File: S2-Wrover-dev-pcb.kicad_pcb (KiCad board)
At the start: 2 copper layers, 99.1 x 50 mm, 6 parts, among them P1 CONN_02X13

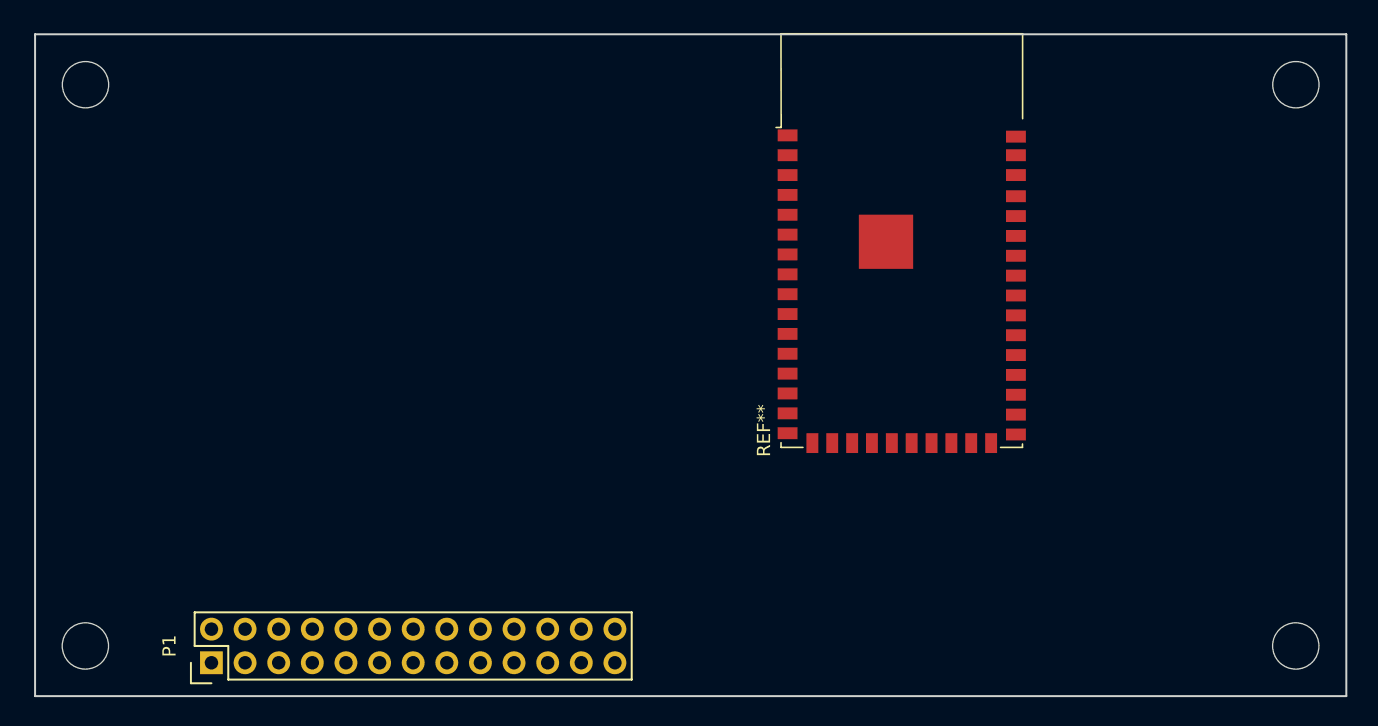
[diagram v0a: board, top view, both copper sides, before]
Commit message: Update schematic and assign footprints
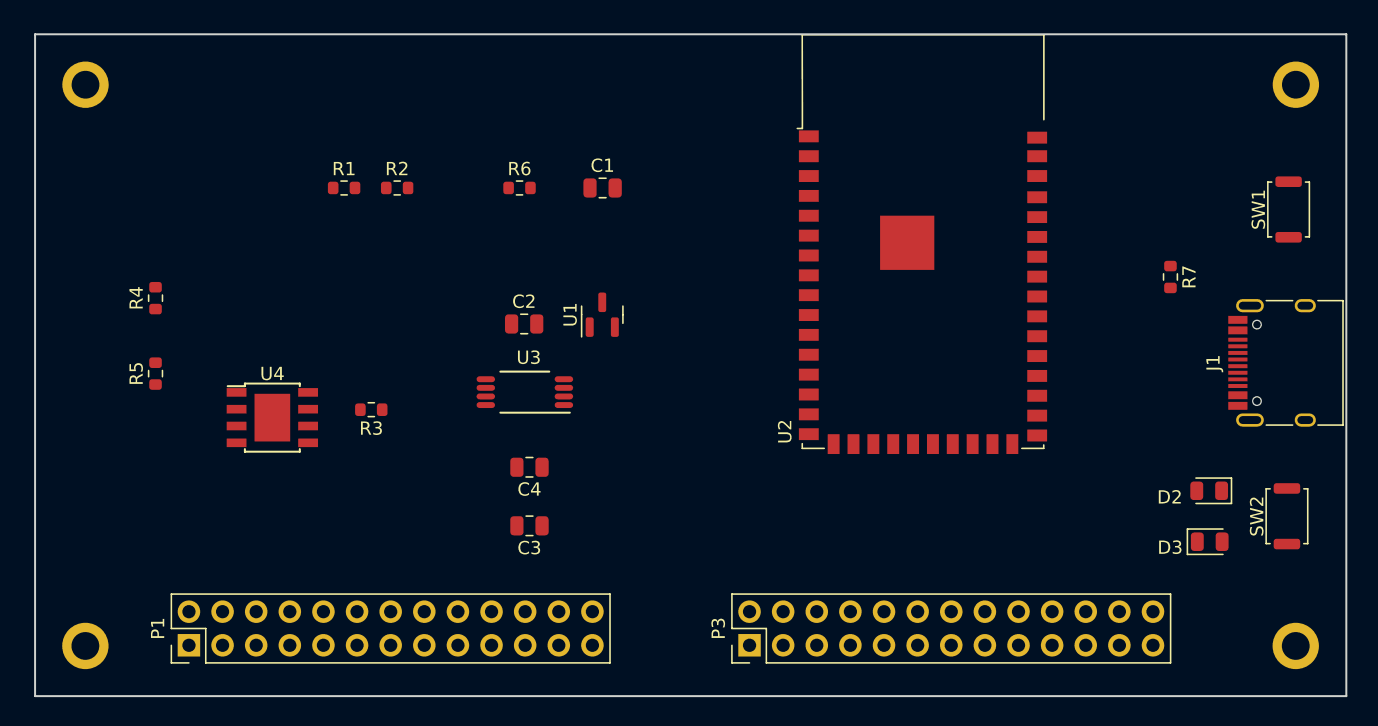
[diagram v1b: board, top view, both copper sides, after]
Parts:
- removed REF**: ESP32-S2-WROVER, footprint:ESP32-S2-WROVER
- added C1: 0.1u, Capacitor_SMD:C_0805_2012Metric, F.Cu at (139.4, 82.7)
- added C2: 100nF, Capacitor_SMD:C_0805_2012Metric, F.Cu at (133.5, 93.0)
- added C3: 100nF, Capacitor_SMD:C_0805_2012Metric, F.Cu at (133.9, 108.3)
- added C4: 100nF, Capacitor_SMD:C_0805_2012Metric, F.Cu at (133.9, 103.8)
- added D2: GRE, LED_SMD:LED_0805_2012Metric, F.Cu at (185.2, 105.6)
- added D3: RED, LED_SMD:LED_0805_2012Metric, F.Cu at (185.3, 109.5)
- added J1: USB_C_Receptacle_USB2.0, footprint:USB_C_Receptacle_HRO_TYPE-C-31-M-12, F.Cu at (191.4, 95.9)
- added P3: CONN_02X13, Connector_PinHeader_2.54mm:PinHeader_2x13_P2.54mm_Vertical, F.Cu at (150.5, 117.3)
- added R1: 10K, Resistor_SMD:R_0603_1608Metric, F.Cu at (119.9, 82.7)
- added R2: 1K, Resistor_SMD:R_0603_1608Metric, F.Cu at (123.9, 82.7)
- added R3: 1K, Resistor_SMD:R_0603_1608Metric, F.Cu at (121.9, 99.5)
- added R4: 400, Resistor_SMD:R_0603_1608Metric, F.Cu at (105.6, 91.1)
- added R5: 6.8K, Resistor_SMD:R_0603_1608Metric, F.Cu at (105.6, 96.8)
- added R6: 5.1k, Resistor_SMD:R_0603_1608Metric, F.Cu at (133.1, 82.7)
- added R7: 5.1k, Resistor_SMD:R_0603_1608Metric, F.Cu at (182.3, 89.5)
- added SW1: RESET, footprint:Alps_SKRK, F.Cu at (191.2, 84.4)
- added SW2: BOOT, footprint:Alps_SKRK, F.Cu at (191.1, 107.5)
- added U1: MCP1700-1202E_SOT23, Package_TO_SOT_SMD:SOT-23, F.Cu at (139.4, 92.3)
- added U2: ESP32-S2-WROVER, RF_Module:ESP32-S2-WROVER, F.Cu at (163.6, 90.6)
- added U3: Val**, footprint:TPS2113APW, F.Cu at (133.5, 98.2)
- added U4: TP4056, TP4056:TP4056_SOP-8-PP, F.Cu at (114.4, 100.1)
- P1: footprint Pin_Headers:Pin_Header_Straight_2x13 -> Connector_PinHeader_2.54mm:PinHeader_2x13_P2.54mm_Vertical
- moved P1 2.15 mm to (108.1, 117.3)
- renumbered MK4 to MK2
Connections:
- P1 pad 1: GND -> BAT-
- P1 pad 10: GPIO_UART1_CTS -> /IO04
- P1 pad 11: GPIO_SPI_CLK -> unconnected-(P1-Pad11)
- P1 pad 12: GPIO_UART1_RTS -> /IO05
- P1 pad 13: GPIO_I2C_SCL -> unconnected-(P1-Pad13)
- P1 pad 14: GPIO_I2S_CLK -> /IO06
- P1 pad 15: GPIO_I2C_SDA -> unconnected-(P1-Pad15)
- P1 pad 16: GPIO_I2S_FRM -> /IO07
- P1 pad 17: GPIO_UART2_TXD -> unconnected-(P1-Pad17)
- P1 pad 18: GPIO_I2S_DO -> /IO08
- P1 pad 19: GPIO_UART2_RXD -> unconnected-(P1-Pad19)
- P1 pad 2: GND -> /3.3v
- P1 pad 20: GPIO_I2S_DI -> /IO09
- P1 pad 21: GPIO_S5_0 -> unconnected-(P1-Pad21)
- P1 pad 22: GPIO_PWM0 -> /IO10
- P1 pad 23: GPIO_S5_1 -> unconnected-(P1-Pad23)
- P1 pad 24: GPIO_PWM1 -> /IO11
- P1 pad 25: GPIO_S5_2 -> unconnected-(P1-Pad25)
- P1 pad 26: I2SMCLK_GPIO -> /IO12
- P1 pad 3: +5V -> unconnected-(P1-Pad3)
- P1 pad 4: +3V3 -> /IO01
- P1 pad 5: GPIO_SPI_CS# -> unconnected-(P1-Pad5)
- P1 pad 6: GPIO_UART1_TXD -> /IO02
- P1 pad 7: GPIO_SPI_MISO -> unconnected-(P1-Pad7)
- P1 pad 8: GPIO_UART1_RXD -> /IO03
- P1 pad 9: GPIO_SPI_MOSI -> unconnected-(P1-Pad9)

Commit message: Update schematic
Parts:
- added J2: Jack-DC, Connector_JST:JST_EH_S2B-EH_1x02_P2.50mm_Horizontal, F.Cu at (112.2, 82.0)
- added P_DEV: CONN_02X13, Connector_PinHeader_2.54mm:PinHeader_2x13_P2.54mm_Vertical, F.Cu at (108.4, 117.3)
- U3: value Val** -> TPS2113APW
- moved C4 13.2 mm to (138.9, 91.6)
- moved C3 13.2 mm to (138.9, 96.1)
- moved R4 9.60 mm to (107.7, 81.7)
- moved R5 9.60 mm to (107.7, 87.4)
- moved R3 9.35 mm to (121.9, 90.1)
- moved U4 9.35 mm to (114.4, 90.7)
- moved U1 8.96 mm to (138.6, 83.4)
- moved C2 8.96 mm to (132.7, 84.1)
- moved U3 8.96 mm to (132.8, 89.2)
- moved P1 6.63 mm to (108.4, 110.7)
- moved D2 4.32 mm to (181.1, 104.4)
- moved D3 4.32 mm to (181.1, 108.3)
- moved R1 4.03 mm to (119.9, 78.7)
- moved R2 4.03 mm to (124.0, 78.7)
- moved C1 3.66 mm to (138.7, 79.1)
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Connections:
- net BAT- renamed GND
- net Net-(U1-Pad3) renamed VIN
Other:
- board text added: "ESP32S2 WROVER SOC idf.py dfu dfu-flash"
- board text added: "FASANI CORPORATION"
- board text added: "FREE AREA"

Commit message: V1 wiring
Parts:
- added C5: 0.1u, Capacitor_SMD:C_0805_2012Metric, F.Cu at (177.0, 78.9)
- moved R1 61.3 mm to (181.2, 80.6)
- moved R2 60.4 mm to (179.3, 102.9), turned to 180 degrees
- moved R3 59.8 mm to (179.8, 105.3), turned to 0 degrees
- moved R6 52.8 mm to (181.7, 98.1)
- moved C1 42.8 mm to (181.3, 83.1), turned to 180 degrees
- moved U1 16.4 mm to (126.5, 94.5)
- moved C3 12.2 mm to (144.3, 85.1)
- moved P3 6.07 mm to (146.0, 113.2)
- moved C4 5.98 mm to (144.3, 89.1)
- moved U4 4.63 mm to (119.1, 90.8), turned to 90 degrees
- moved J2 3.98 mm to (116.2, 81.7)
- moved R5 3.65 mm to (111.3, 88.0)
- moved R4 3.65 mm to (111.3, 82.3)
- moved U3 2.48 mm to (132.9, 91.7), turned to 90 degrees
- moved D3 2.35 mm to (183.2, 107.2)
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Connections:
- P3 pad 10: /IO15 -> /IO17
- P3 pad 12: /IO16 -> /IO18
- P3 pad 14: /IO17 -> /IO21
- P3 pad 16: /IO21 -> /IO33
- P3 pad 18: /IO33 -> /IO34
- P3 pad 20: /IO34 -> /IO35
- P3 pad 22: /IO35 -> /IO36
- P3 pad 24: /IO36 -> /IO37
- P3 pad 26: /IO37 -> unconnected-(P3-Pad26)
- P3 pad 8: /IO14 -> /IO16
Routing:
- net GND: track 0.00 -> 157.4 mm, vias 0 -> 6
- net Net-(R3-Pad2): track 0.00 -> 154.7 mm, vias 0 -> 4
- net VBUS: track 0.00 -> 153.3 mm, vias 0 -> 6
- net /3.3v: track 0.00 -> 131.6 mm, vias 0 -> 5
- net /IO46: track 0.00 -> 85.5 mm, vias 0 -> 1
- net Net-(R2-Pad2): track 0.00 -> 84.9 mm, vias 0 -> 2
- net /IO45: track 0.00 -> 80.5 mm, vias 0 -> 1
- net /IO41: track 0.00 -> 77.8 mm, vias 0 -> 2
- net BOOT_MODE: track 0.00 -> 72.2 mm, vias 0 -> 4
- net /IO42: track 0.00 -> 67.5 mm, vias 0 -> 2
- net /IO40: track 0.00 -> 66.3 mm, vias 0 -> 2
- net /RX: track 0.00 -> 59.9 mm, vias 0 -> 1
- net /IO01: track 0.00 -> 56.4 mm
- net /IO02: track 0.00 -> 53.5 mm
- net /TX: track 0.00 -> 51.2 mm, vias 0 -> 1
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
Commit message: Passing DRC
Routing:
- net GND: track 157.4 -> 196.5 mm, vias 6 -> 13
- net VBUS: track 153.3 -> 150.7 mm
- net /IO10: track 29.7 -> 28.4 mm
- net /IO16: track 12.0 -> 11.2 mm
- net /IO12: track 23.2 -> 22.4 mm
- net /IO15: track 12.3 -> 11.6 mm
- net /IO13: track 15.6 -> 14.9 mm
- net /IO14: track 13.6 -> 13.0 mm
- net /IO08: track 36.3 -> 35.7 mm
- net /IO42: track 67.5 -> 68.0 mm
- added copper zone on B.Cu, net GND
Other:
- outline, holes or cut-outs redrawn

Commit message: Make only one big GND pane in bottom layer
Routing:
- net GND: vias 13 -> 16
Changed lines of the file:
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@@
       (effects (font (size 1 1) (thickness 0.15)))
     )
-    (fp_text value "ESP32-S2-WROVER" (at 0.145 -8.075 180) (layer "F.Fab")
+    (fp_text value "ESP32-S2-WROVER" (at 0.22 -13.8 180) (layer "F.Fab")
       (effects (font (size 1 1) (thickness 0.15)))
     )
@@
   (segment (start 187.385 92.5375) (end 188.3 91.6225) (width 0.4) (layer "F.Cu") (net 1))
   (via (at 132.12 96.005) (size 0.6) (drill 0.4) (layers "F.Cu" "B.Cu") (net 1))
+  (via (at 161.42 86.78) (size 0.8) (drill 0.6) (layers "F.Cu" "B.Cu") (net 1))
   (via (at 133.77 81.78) (size 0.6) (drill 0.4) (layers "F.Cu" "B.Cu") (net 1))
   (via (at 140.845 108.805) (size 0.6) (drill 0.4) (layers "F.Cu" "B.Cu") (net 1))
@@
   (via (at 183.77 94.555) (size 0.6) (drill 0.4) (layers "F.Cu" "B.Cu") (net 1))
   (via (at 108.595 87.08) (size 0.6) (drill 0.4) (layers "F.Cu" "B.Cu") (net 1))
+  (via (at 162.4575 86.78) (size 0.8) (drill 0.6) (layers "F.Cu" "B.Cu") (net 1))
   (via (at 183.995 82.605) (size 0.6) (drill 0.4) (layers "F.Cu" "B.Cu") (net 1))
   (via (at 134.745 87.43) (size 0.6) (drill 0.4) (layers "F.Cu" "B.Cu") (net 1))
   (via (at 184.5575 92.6925) (size 0.6) (drill 0.4) (layers "F.Cu" "B.Cu") (net 1))
+  (via (at 163.495 86.805) (size 0.8) (drill 0.6) (layers "F.Cu" "B.Cu") (net 1))
   (segment (start 113.92 87.13) (end 108.645 87.13) (width 0.3) (layer "B.Cu") (net 1))
   (segment (start 132.12 96.005) (end 129.595 96.005) (width 0.4) (layer "B.Cu") (net 1))
@@
   (segment (start 191.195 90.48) (end 191.195 109.555) (width 0.25) (layer "B.Cu") (net 55))
   (zone (net 1) (net_name "GND") (layer "B.Cu") (hatch edge 0.508)
-    (connect_pads (clearance 0))
+    (connect_pads (clearance 0.4))
     (min_thickness 0.254) (filled_areas_thickness no)
     (fill yes (thermal_gap 0.508) (thermal_bridge_width 0.508))
     (polygon
       (pts
-        (xy 153.47 108.905)
+        (xy 195.97 121.355)
+        (xy 178.245 121.33)
+        (xy 178.245 108.78)
+        (xy 170.3575 108.78)
         (xy 144.845 108.905)
         (xy 144.595 114.105)
@@
         (xy 95.92 109.155)
         (xy 95.87 70.53)
-        (xy 153.52 70.68)
+        (xy 195.895 70.555)
       )
     )
-  )
-  (zone (net 1) (net_name "GND") (layer "B.Cu") (hatch edge 0.508)
-    (connect_pads (clearance 0))
-    (min_thickness 0.254) (filled_areas_thickness no)
-    (fill yes (thermal_gap 0.508) (thermal_bridge_width 0.508))
-    (polygon
-      (pts
-        (xy 195.67 121.305)
-        (xy 178.17 121.055)
-        (xy 178.17 108.93)
-        (xy 174.445 106.33)
-        (xy 174.345 71.105)
-        (xy 195.545 71.055)
-      )
-    )
